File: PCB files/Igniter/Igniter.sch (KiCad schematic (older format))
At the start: 21 parts, among them IC1 74HC4050, J1 Micro_SD_Card, J2 Battery +, J3 Battery -, J5 PT, J6 Ignition Coil +, J7 Ignition coil -, Q1 N MOSFET, SW1 ARM

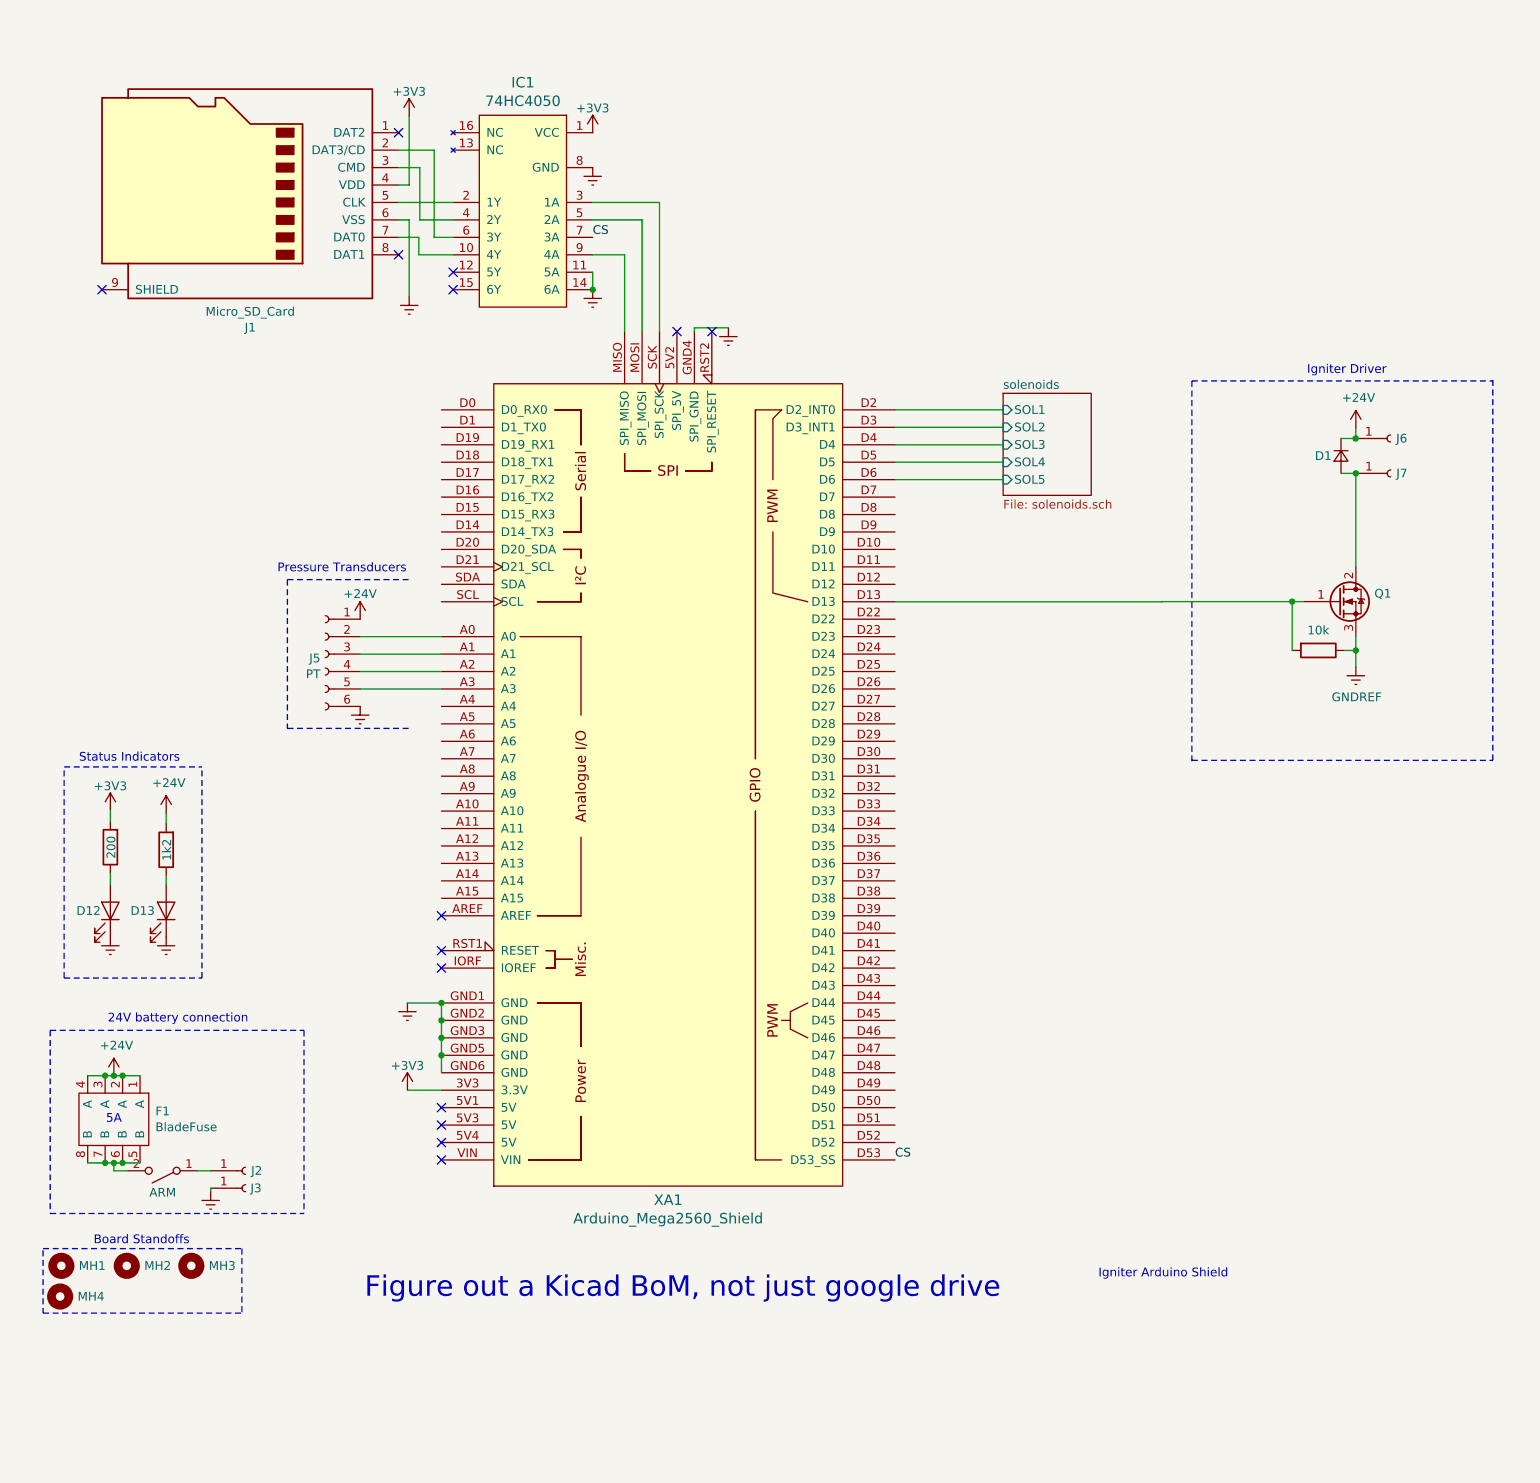
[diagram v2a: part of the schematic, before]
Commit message: 12/9/2019
Schematic
-Removed SOL bus connector, changed to individual circuits
-Removed pressure transducer shared connector. changed back to individual circuits
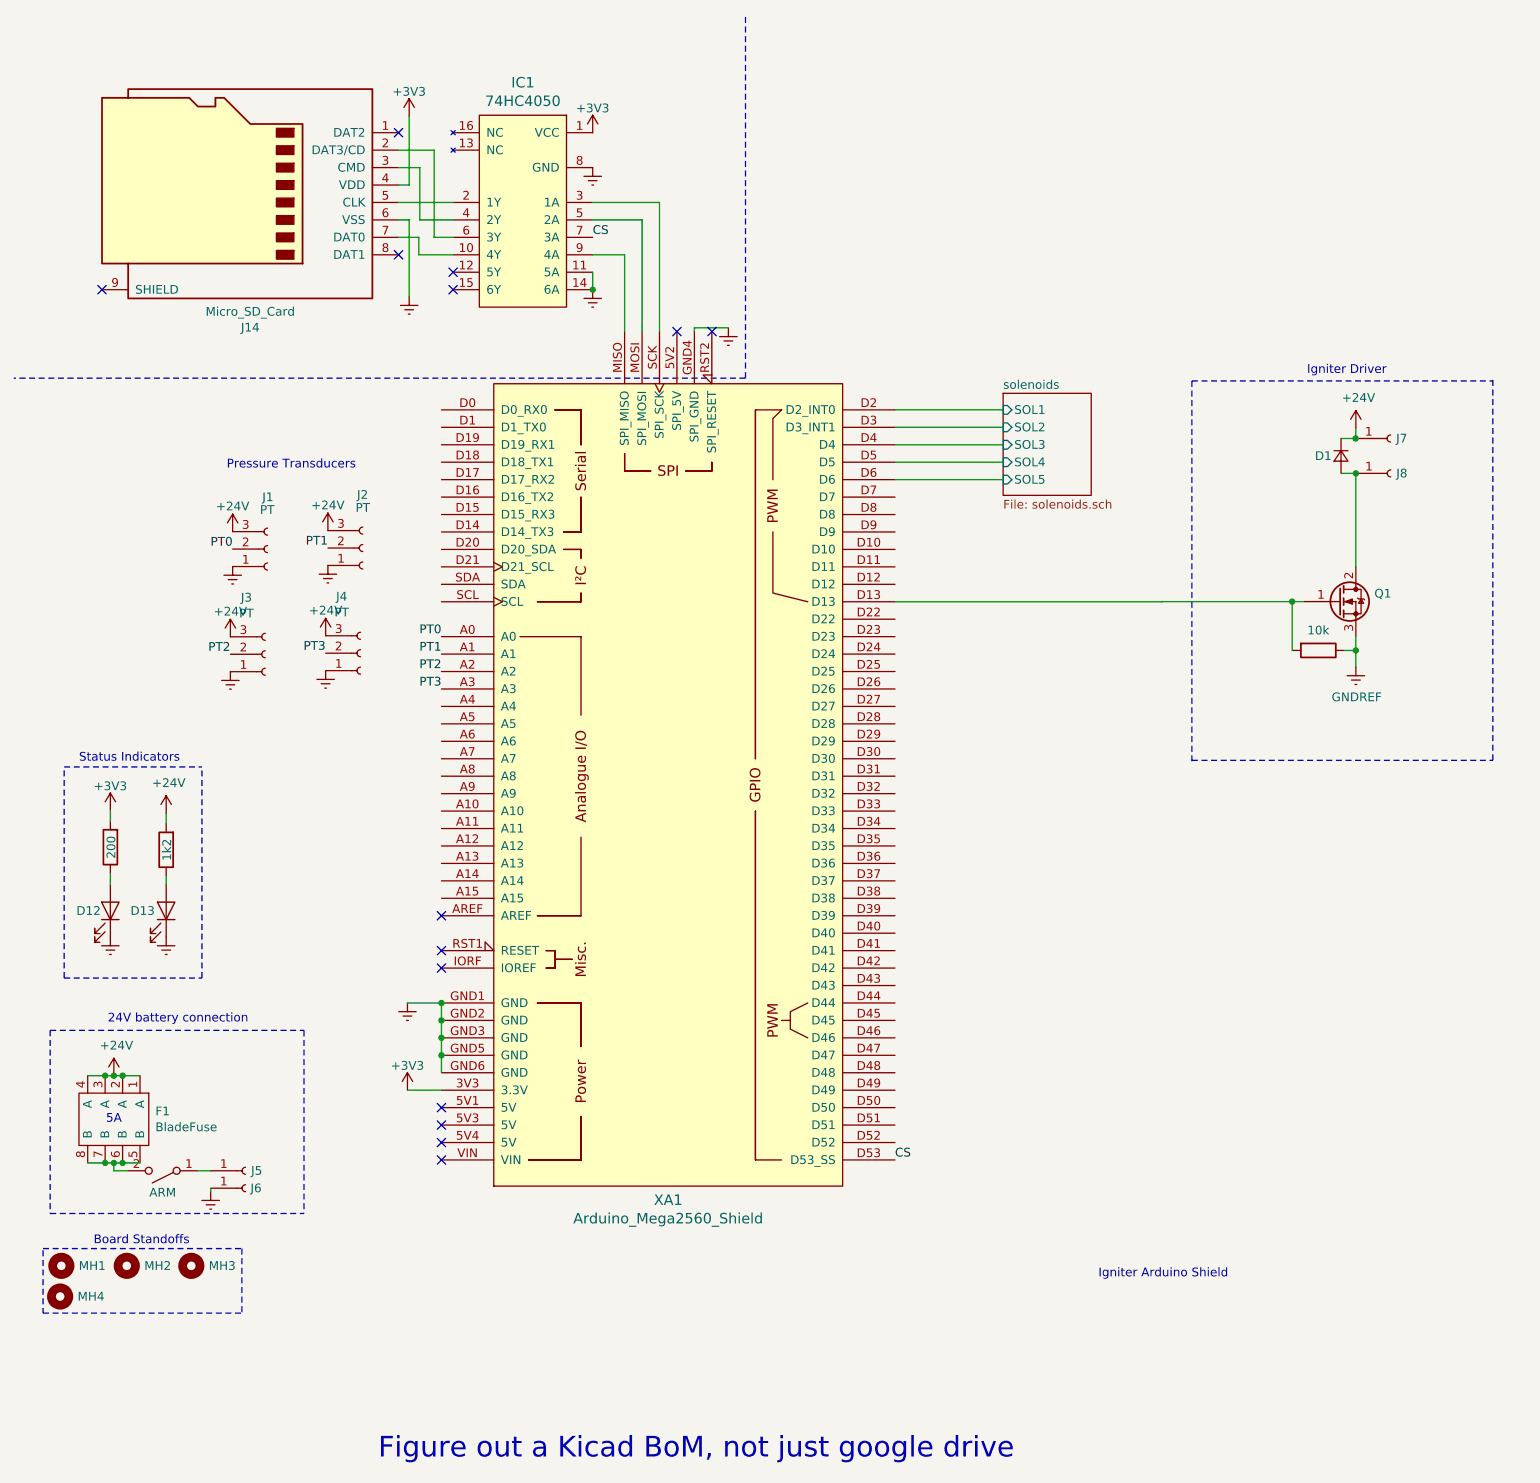
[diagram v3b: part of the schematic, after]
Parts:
- removed J5: PT, Connector_Dsub:DSUB-9_Male_Horizontal_P2.77x2.54mm_EdgePinOffset9.40mm, symbol Connector:Conn_01x06_Female
- added J1, J2, J3, J4: PT, Connector_Molex:Molex_Nano-Fit_105309-xx03_1x03_P2.50mm_Vertical, symbol Connector:Conn_01x03_Female
- renumbered J1 to J14, J2 to J5, J3 to J6, J6 to J7, J7 to J8
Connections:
- net +24V: now also J1.3 (Pin_3), J2.3 (Pin_3), J3.3 (Pin_3), J4.3 (Pin_3)
- net GNDREF: now also J1.1 (Pin_1), J2.1 (Pin_1), J3.1 (Pin_1), J4.1 (Pin_1)
- net PT0: now reaches XA1.A0
- net PT0: now also J1.2 (Pin_2)
- net PT1: now reaches XA1.A1
- net PT1: now also J2.2 (Pin_2)
- net PT2: now reaches XA1.A2
- net PT2: now also J3.2 (Pin_2)
- net PT3: now reaches XA1.A3
- net PT3: now also J4.2 (Pin_2)
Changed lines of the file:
@@
 LIBS:interface
 LIBS:Igniter-cache
-EELAYER 26 0
+EELAYER 29 0
 EELAYER END
 $Descr A 11000 8500
@@
 Wire Notes Line
 	640  7550 1780 7550
-Text Notes 6130 7845 2    118  ~ 0
+Text Notes 6208 8766 2    118  ~ 0
 Figure out a Kicad BoM, not just google drive
-Wire Wire Line
-	2924 4342 2458 4342
-Wire Wire Line
-	2458 4242 2924 4242
-Wire Wire Line
-	2458 4042 2924 4042
-Wire Wire Line
-	2458 4142 2924 4142
-Wire Notes Line
-	2232 4602 2232 4601
-Wire Notes Line
-	2041 4568 2745 4568
-Wire Notes Line
-	2041 3715 2746 3715
-Wire Notes Line
-	2041 3715 2041 4568
-$Comp
-L power:GNDREF #PWR012
-U 1 1 5DEBAFC0
-P 2458 4442
-F 0 "#PWR012" H 2458 4192 50  0001 C CNN
-F 1 "GNDREF" H 2463 4269 50  0001 C CNN
-F 2 "" H 2458 4442 50  0001 C CNN
-F 3 "" H 2458 4442 50  0001 C CNN
-	1    2458 4442
-	-1   0    0    -1
-$EndComp
-$Comp
-L power:+24V #PWR07
-U 1 1 5DEBA11C
-P 2458 3942
-F 0 "#PWR07" H 2458 3792 50  0001 C CNN
-F 1 "+24V" H 2458 4087 50  0000 C CNN
-F 2 "" H 2458 3942 50  0001 C CNN
-F 3 "" H 2458 3942 50  0001 C CNN
-	1    2458 3942
-	-1   0    0    -1
-$EndComp
-$Comp
-L Connector:Conn_01x06_Female J5
-U 1 1 5DEB9566
-P 2258 4142
-F 0 "J5" H 2286 4118 50  0000 L CNN
-F 1 "PT" H 2286 4027 50  0000 L CNN
-F 2 "Connector_Dsub:DSUB-9_Male_Horizontal_P2.77x2.54mm_EdgePinOffset9.40mm" H 2258 4142 50  0001 C CNN
-F 3 "~" H 2258 4142 50  0001 C CNN
-	1    2258 4142
-	-1   0    0    -1
-$EndComp
 Wire Wire Line
 	7801 3841 7866 3841
@@
 Wire Wire Line
 	5524 2742 6144 2742
-Text Notes 1983 3683 0    50   ~ 0
-Pressure Transducers
 $Sheet
 S 6144 2647 505  585
@@
 P 1778 1453
 AR Path="/5DC64D13/5DF09A80" Ref="J?"  Part="1"
-AR Path="/5DF09A80" Ref="J1"  Part="1"
-F 0 "J1" H 1728 636 50  0000 C CNN
+AR Path="/5DF09A80" Ref="J14"  Part="1"
+F 0 "J14" H 1728 636 50  0000 C CNN
 F 1 "Micro_SD_Card" H 1728 727 50  0000 C CNN
 F 2 "Connector_Card:microSD_HC_Hirose_DM3BT-DSF-PEJS" H 2928 1753 50  0001 C CNN
@@
 	4174 1553 4174 2292
 $Comp
-L Connector:Conn_01x01_Female J2
+L Connector:Conn_01x01_Female J5
 U 1 1 5DEA7B33
 P 1801 7104
-F 0 "J2" H 1833 7104 50  0000 L CNN
+F 0 "J5" H 1833 7104 50  0000 L CNN
 F 1 "Battery +" H 1828 7039 50  0001 L CNN
 F 2 "IgniterCustom:BananaJack15.5mm" H 1801 7104 50  0001 C CNN
@@
 $EndComp
 $Comp
-L Connector:Conn_01x01_Female J3
+L Connector:Conn_01x01_Female J6
 U 1 1 5DEA7B7D
 P 1801 7204
-F 0 "J3" H 1829 7204 50  0000 L CNN
+F 0 "J6" H 1829 7204 50  0000 L CNN
 F 1 "Battery -" H 1828 7139 50  0001 L CNN
 F 2 "IgniterCustom:BananaJack15.5mm" H 1801 7204 50  0001 C CNN
@@
 $EndComp
 $Comp
-L Connector:Conn_01x01_Female J6
+L Connector:Conn_01x01_Female J7
 U 1 1 5DEA8937
 P 8365 2906
-F 0 "J6" H 8397 2906 50  0000 L CNN
+F 0 "J7" H 8397 2906 50  0000 L CNN
 F 1 "Ignition Coil +" H 8392 2841 50  0001 L CNN
 F 2 "IgniterCustom:BananaJack15.5mm" H 8365 2906 50  0001 C CNN
@@
 	8165 2906 8166 2906
 $Comp
-L Connector:Conn_01x01_Female J7
+L Connector:Conn_01x01_Female J8
 U 1 1 5DEA8AF3
 P 8366 3106
-F 0 "J7" H 8398 3106 50  0000 L CNN
+F 0 "J8" H 8398 3106 50  0000 L CNN
 F 1 "Ignition coil -" H 8393 3041 50  0001 L CNN
 F 2 "IgniterCustom:BananaJack15.5mm" H 8366 3106 50  0001 C CNN
@@
 NoConn ~ 4274 2293
 NoConn ~ 4475 2293
+Text Notes 1693 3088 0    50   ~ 0
+Pressure Transducers
+$Comp
+L power:GNDREF #PWR0118
+U 1 1 5DFAB89C
+P 1727 3640
+AR Path="/5DFAB89C" Ref="#PWR0118"  Part="1"
+AR Path="/5DB4D508/5DFAB89C" Ref="#PWR?"  Part="1"
+F 0 "#PWR0118" H 1727 3390 50  0001 C CNN
+F 1 "GNDREF" H 1732 3467 50  0001 C CNN
+F 2 "" H 1727 3640 50  0001 C CNN
+F 3 "" H 1727 3640 50  0001 C CNN
+	1    1727 3640
+	-1   0    0    -1
+$EndComp
+$Comp
+L Connector:Conn_01x03_Female J?
+U 1 1 5DFAB896
+P 1927 3540
+AR Path="/5DB4D508/5DFAB896" Ref="J?"  Part="1"
+AR Path="/5DFAB896" Ref="J1"  Part="1"
+F 0 "J1" H 1929 3242 50  0000 C CNN
+F 1 "PT" H 1925 3315 50  0000 C CNN
+F 2 "Connector_Molex:Molex_Nano-Fit_105309-xx03_1x03_P2.50mm_Vertical" H 1927 3540 50  0001 C CNN
+F 3 "~" H 1927 3540 50  0001 C CNN
+	1    1927 3540
+	1    0    0    1
+$EndComp
+$Comp
+L power:GNDREF #PWR0119
+U 1 1 5DFB1672
+P 1714 4243
+AR Path="/5DFB1672" Ref="#PWR0119"  Part="1"
+AR Path="/5DB4D508/5DFB1672" Ref="#PWR?"  Part="1"
+F 0 "#PWR0119" H 1714 3993 50  0001 C CNN
+F 1 "GNDREF" H 1719 4070 50  0001 C CNN
+F 2 "" H 1714 4243 50  0001 C CNN
+F 3 "" H 1714 4243 50  0001 C CNN
+	1    1714 4243
+	-1   0    0    -1
+$EndComp
+$Comp
+L Connector:Conn_01x03_Female J?
+U 1 1 5DFB167C
+P 1914 4143
+AR Path="/5DB4D508/5DFB167C" Ref="J?"  Part="1"
+AR Path="/5DFB167C" Ref="J3"  Part="1"
+F 0 "J3" H 1806 3818 50  0000 C CNN
+F 1 "PT" H 1806 3909 50  0000 C CNN
+F 2 "Connector_Molex:Molex_Nano-Fit_105309-xx03_1x03_P2.50mm_Vertical" H 1914 4143 50  0001 C CNN
+F 3 "~" H 1914 4143 50  0001 C CNN
+	1    1914 4143
+	1    0    0    1
+$EndComp
+$Comp
+L power:GNDREF #PWR0120
+U 1 1 5DFB50AD
+P 2273 3634
+AR Path="/5DFB50AD" Ref="#PWR0120"  Part="1"
+AR Path="/5DB4D508/5DFB50AD" Ref="#PWR?"  Part="1"
+F 0 "#PWR0120" H 2273 3384 50  0001 C CNN
+F 1 "GNDREF" H 2278 3461 50  0001 C CNN
+F 2 "" H 2273 3634 50  0001 C CNN
+F 3 "" H 2273 3634 50  0001 C CNN
+	1    2273 3634
+	-1   0    0    -1
+$EndComp
+$Comp
+L Connector:Conn_01x03_Female J?
+U 1 1 5DFB50B7
+P 2473 3534
+AR Path="/5DB4D508/5DFB50B7" Ref="J?"  Part="1"
+AR Path="/5DFB50B7" Ref="J2"  Part="1"
+F 0 "J2" H 2472 3229 50  0000 C CNN
+F 1 "PT" H 2473 3303 50  0000 C CNN
+F 2 "Connector_Molex:Molex_Nano-Fit_105309-xx03_1x03_P2.50mm_Vertical" H 2473 3534 50  0001 C CNN
+F 3 "~" H 2473 3534 50  0001 C CNN
+	1    2473 3534
+	1    0    0    1
+$EndComp
+$Comp
+L power:GNDREF #PWR0121
+U 1 1 5DFB50C1
+P 2260 4237
+AR Path="/5DFB50C1" Ref="#PWR0121"  Part="1"
+AR Path="/5DB4D508/5DFB50C1" Ref="#PWR?"  Part="1"
+F 0 "#PWR0121" H 2260 3987 50  0001 C CNN
+F 1 "GNDREF" H 2265 4064 50  0001 C CNN
+F 2 "" H 2260 4237 50  0001 C CNN
+F 3 "" H 2260 4237 50  0001 C CNN
+	1    2260 4237
+	-1   0    0    -1
+$EndComp
+$Comp
+L Connector:Conn_01x03_Female J?
+U 1 1 5DFB50CB
+P 2460 4137
+AR Path="/5DB4D508/5DFB50CB" Ref="J?"  Part="1"
+AR Path="/5DFB50CB" Ref="J4"  Part="1"
+F 0 "J4" H 2352 3812 50  0000 C CNN
+F 1 "PT" H 2352 3903 50  0000 C CNN
+F 2 "Connector_Molex:Molex_Nano-Fit_105309-xx03_1x03_P2.50mm_Vertical" H 2460 4137 50  0001 C CNN
+F 3 "~" H 2460 4137 50  0001 C CNN
+	1    2460 4137
+	1    0    0    1
+$EndComp
+Wire Notes Line
+	4667 2560 472  2560
+Wire Notes Line
+	4667 2560 4667 471
+$Comp
+L power:+24V #PWR0122
+U 1 1 5DFBEE1E
+P 1727 3440
+F 0 "#PWR0122" H 1727 3290 50  0001 C CNN
+F 1 "+24V" H 1727 3585 50  0000 C CNN
+F 2 "" H 1727 3440 50  0001 C CNN
+F 3 "" H 1727 3440 50  0001 C CNN
+	1    1727 3440
+	-1   0    0    -1
+$EndComp
+Text Label 2924 4042 2    50   ~ 0
+PT0
+Text Label 2924 4142 2    50   ~ 0
+PT1
+Text Label 2924 4242 2    50   ~ 0
+PT2
+Text Label 2924 4342 2    50   ~ 0
+PT3
+Text Label 1727 3540 2    50   ~ 0
+PT0
+Text Label 2273 3534 2    50   ~ 0
+PT1
+Text Label 1714 4143 2    50   ~ 0
+PT2
+Text Label 2260 4137 2    50   ~ 0
+PT3
+$Comp
+L power:+24V #PWR0123
+U 1 1 5DFC5913
+P 2273 3434
+F 0 "#PWR0123" H 2273 3284 50  0001 C CNN
+F 1 "+24V" H 2273 3579 50  0000 C CNN
+F 2 "" H 2273 3434 50  0001 C CNN
+F 3 "" H 2273 3434 50  0001 C CNN
+	1    2273 3434
+	-1   0    0    -1
+$EndComp
+$Comp
+L power:+24V #PWR0124
+U 1 1 5DFD2F0A
+P 1714 4043
+F 0 "#PWR0124" H 1714 3893 50  0001 C CNN
+F 1 "+24V" H 1714 4188 50  0000 C CNN
+F 2 "" H 1714 4043 50  0001 C CNN
+F 3 "" H 1714 4043 50  0001 C CNN
+	1    1714 4043
+	-1   0    0    -1
+$EndComp
+$Comp
+L power:+24V #PWR0125
+U 1 1 5DFD3DEC
+P 2260 4037
+F 0 "#PWR0125" H 2260 3887 50  0001 C CNN
+F 1 "+24V" H 2260 4182 50  0000 C CNN
+F 2 "" H 2260 4037 50  0001 C CNN
+F 3 "" H 2260 4037 50  0001 C CNN
+	1    2260 4037
+	-1   0    0    -1
+$EndComp
 $EndSCHEMATC

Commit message: 12/9/2019
-Picked SPOX vertical molex for pressure transducer connnector
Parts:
- J1, J2, J3, J4: footprint Connector_Molex:Molex_Nano-Fit_105309-xx03_1x03_P2.50mm_Vertical -> Connector_Molex:Molex_SPOX_5267-03A_1x03_P2.50mm_Vertical
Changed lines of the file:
@@
 F 0 "J1" H 1929 3242 50  0000 C CNN
 F 1 "PT" H 1925 3315 50  0000 C CNN
-F 2 "Connector_Molex:Molex_Nano-Fit_105309-xx03_1x03_P2.50mm_Vertical" H 1927 3540 50  0001 C CNN
+F 2 "Connector_Molex:Molex_SPOX_5267-03A_1x03_P2.50mm_Vertical" H 1927 3540 50  0001 C CNN
 F 3 "~" H 1927 3540 50  0001 C CNN
 	1    1927 3540
@@
 F 0 "J3" H 1806 3818 50  0000 C CNN
 F 1 "PT" H 1806 3909 50  0000 C CNN
-F 2 "Connector_Molex:Molex_Nano-Fit_105309-xx03_1x03_P2.50mm_Vertical" H 1914 4143 50  0001 C CNN
+F 2 "Connector_Molex:Molex_SPOX_5267-03A_1x03_P2.50mm_Vertical" H 1914 4143 50  0001 C CNN
 F 3 "~" H 1914 4143 50  0001 C CNN
 	1    1914 4143
@@
 F 0 "J2" H 2472 3229 50  0000 C CNN
 F 1 "PT" H 2473 3303 50  0000 C CNN
-F 2 "Connector_Molex:Molex_Nano-Fit_105309-xx03_1x03_P2.50mm_Vertical" H 2473 3534 50  0001 C CNN
+F 2 "Connector_Molex:Molex_SPOX_5267-03A_1x03_P2.50mm_Vertical" H 2473 3534 50  0001 C CNN
 F 3 "~" H 2473 3534 50  0001 C CNN
 	1    2473 3534
@@
 F 0 "J4" H 2352 3812 50  0000 C CNN
 F 1 "PT" H 2352 3903 50  0000 C CNN
-F 2 "Connector_Molex:Molex_Nano-Fit_105309-xx03_1x03_P2.50mm_Vertical" H 2460 4137 50  0001 C CNN
+F 2 "Connector_Molex:Molex_SPOX_5267-03A_1x03_P2.50mm_Vertical" H 2460 4137 50  0001 C CNN
 F 3 "~" H 2460 4137 50  0001 C CNN
 	1    2460 4137

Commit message: 12/10/2019
-Selected battery molex connector footprint
-Read netlist
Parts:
- removed J5: Battery +, IgniterCustom:BananaJack15.5mm, symbol Connector:Conn_01x01_Female
- removed J6: Battery -, IgniterCustom:BananaJack15.5mm, symbol Connector:Conn_01x01_Female
- added J5: Battery, Connector_Molex:Molex_Mini-Fit_Jr_5566-02A_2x01_P4.20mm_Vertical, symbol Connector:Conn_01x02_Female
- renumbered J14 to J13, J7 to J6, J8 to J7
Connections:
- net GNDREF: now also J5.2 (Pin_2)
- net at SW1.1 (A): now also J5.1 (Pin_1)
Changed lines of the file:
@@
 P 1778 1453
 AR Path="/5DC64D13/5DF09A80" Ref="J?"  Part="1"
-AR Path="/5DF09A80" Ref="J14"  Part="1"
-F 0 "J14" H 1728 636 50  0000 C CNN
+AR Path="/5DF09A80" Ref="J13"  Part="1"
+F 0 "J13" H 1728 636 50  0000 C CNN
 F 1 "Micro_SD_Card" H 1728 727 50  0000 C CNN
 F 2 "Connector_Card:microSD_HC_Hirose_DM3BT-DSF-PEJS" H 2928 1753 50  0001 C CNN
@@
 	4174 1553 4174 2292
 $Comp
-L Connector:Conn_01x01_Female J5
-U 1 1 5DEA7B33
-P 1801 7104
-F 0 "J5" H 1833 7104 50  0000 L CNN
-F 1 "Battery +" H 1828 7039 50  0001 L CNN
-F 2 "IgniterCustom:BananaJack15.5mm" H 1801 7104 50  0001 C CNN
-F 3 "~" H 1801 7104 50  0001 C CNN
-	1    1801 7104
-	1    0    0    -1
-$EndComp
-$Comp
 L Connector:Conn_01x01_Female J6
-U 1 1 5DEA7B7D
-P 1801 7204
-F 0 "J6" H 1829 7204 50  0000 L CNN
-F 1 "Battery -" H 1828 7139 50  0001 L CNN
-F 2 "IgniterCustom:BananaJack15.5mm" H 1801 7204 50  0001 C CNN
-F 3 "~" H 1801 7204 50  0001 C CNN
-	1    1801 7204
-	1    0    0    -1
-$EndComp
-$Comp
-L Connector:Conn_01x01_Female J7
 U 1 1 5DEA8937
 P 8365 2906
-F 0 "J7" H 8397 2906 50  0000 L CNN
+F 0 "J6" H 8397 2906 50  0000 L CNN
 F 1 "Ignition Coil +" H 8392 2841 50  0001 L CNN
 F 2 "IgniterCustom:BananaJack15.5mm" H 8365 2906 50  0001 C CNN
@@
 	8165 2906 8166 2906
 $Comp
-L Connector:Conn_01x01_Female J8
+L Connector:Conn_01x01_Female J7
 U 1 1 5DEA8AF3
 P 8366 3106
-F 0 "J8" H 8398 3106 50  0000 L CNN
+F 0 "J7" H 8398 3106 50  0000 L CNN
 F 1 "Ignition coil -" H 8393 3041 50  0001 L CNN
 F 2 "IgniterCustom:BananaJack15.5mm" H 8366 3106 50  0001 C CNN
@@
 	-1   0    0    -1
 $EndComp
+$Comp
+L Connector:Conn_01x02_Female J5
+U 1 1 5DF0B34B
+P 1801 7104
+F 0 "J5" H 1829 7080 50  0000 L CNN
+F 1 "Battery" H 1829 6989 50  0000 L CNN
+F 2 "Connector_Molex:Molex_Mini-Fit_Jr_5566-02A_2x01_P4.20mm_Vertical" H 1801 7104 50  0001 C CNN
+F 3 "~" H 1801 7104 50  0001 C CNN
+	1    1801 7104
+	1    0    0    -1
+$EndComp
 $EndSCHEMATC
